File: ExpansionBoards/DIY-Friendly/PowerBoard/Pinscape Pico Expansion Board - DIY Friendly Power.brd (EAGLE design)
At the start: 138 x 102 mm, 87 parts, among them IC1 UCC27524P, IC10 ULN2803A, IC11 ULN2803A, IC12 ULN2803A, IC13 DS1307+, IC2 UCC27524P, IC3 UCC27524P, IC4 UCC27524P, IC5 UCC27524P, IC6 UCC27524P, IC7 UCC27524P, IC8 UCC27524P, IC9 ULN2803A, J1 640445-9, J2 640445-9, J3 640445-6, J4 1-640456-0, J5 1-640456-0, J6 1-640456-0, J7 1-640456-0, Q1 FDPF085N10A, Q10 FDPF085N10A, Q11 FDPF085N10A, Q12 FDPF085N10A, Q13 FDPF085N10A, Q14 FDPF085N10A, Q15 FDPF085N10A, Q16 FDPF085N10A, Q17 2N2222A, Q18 2N2222A, Q2 FDPF085N10A, Q3 FDPF085N10A, Q4 FDPF085N10A, Q5 FDPF085N10A, Q6 FDPF085N10A, Q7 FDPF085N10A, Q8 FDPF085N10A, Q9 FDPF085N10A, Y1 ECS-.327-12.5-13X-C

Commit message: BOM tweaks
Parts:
- Q1, Q10, Q11, Q12, Q13, Q14, Q15, Q16, Q2, Q3, Q4, Q5, Q6, Q7, Q8, Q9: value FDPF085N10A -> STP19NF20
- R1, R10, R11, R12, R14, R15, R16, R17, R2, R3, R4, R5, R6, R7, R8, R9: value 4R7 -> 200R

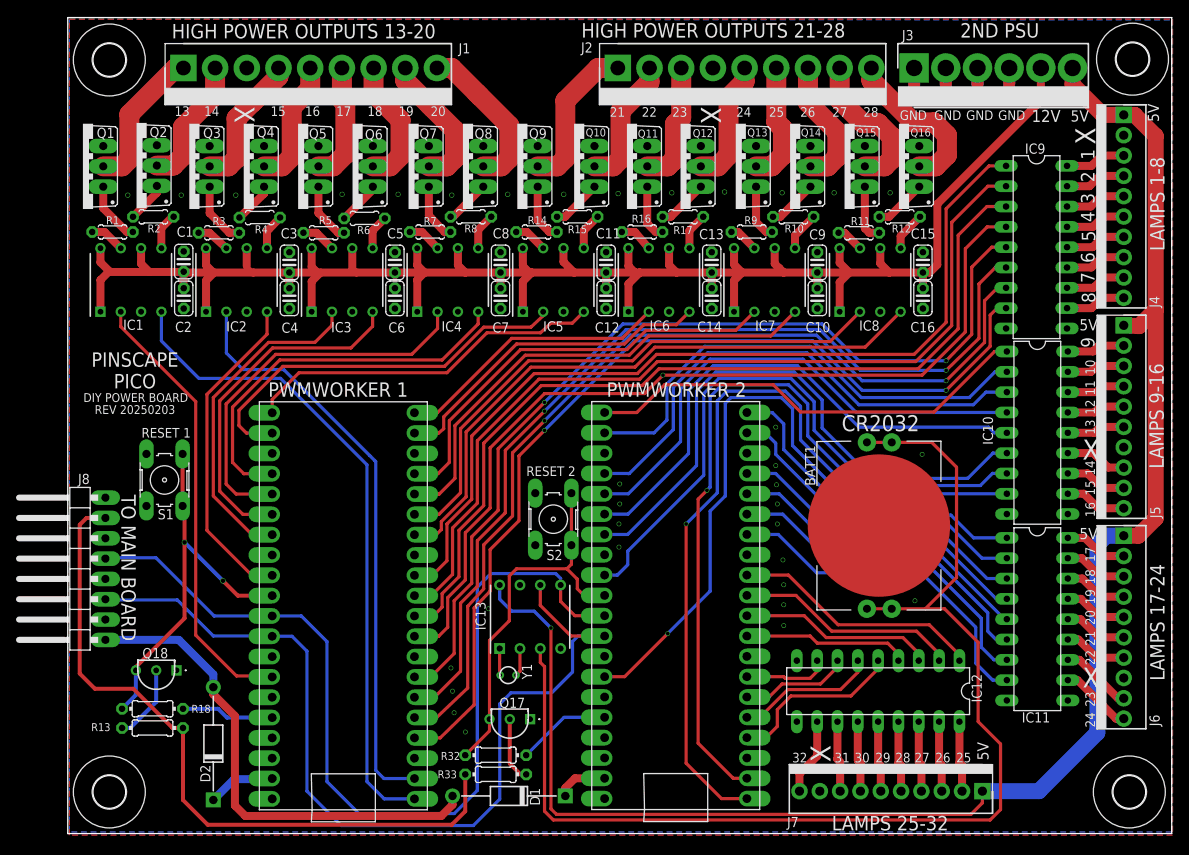
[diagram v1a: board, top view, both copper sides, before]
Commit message: exp board: DIY power: change battery holder to snap-in type
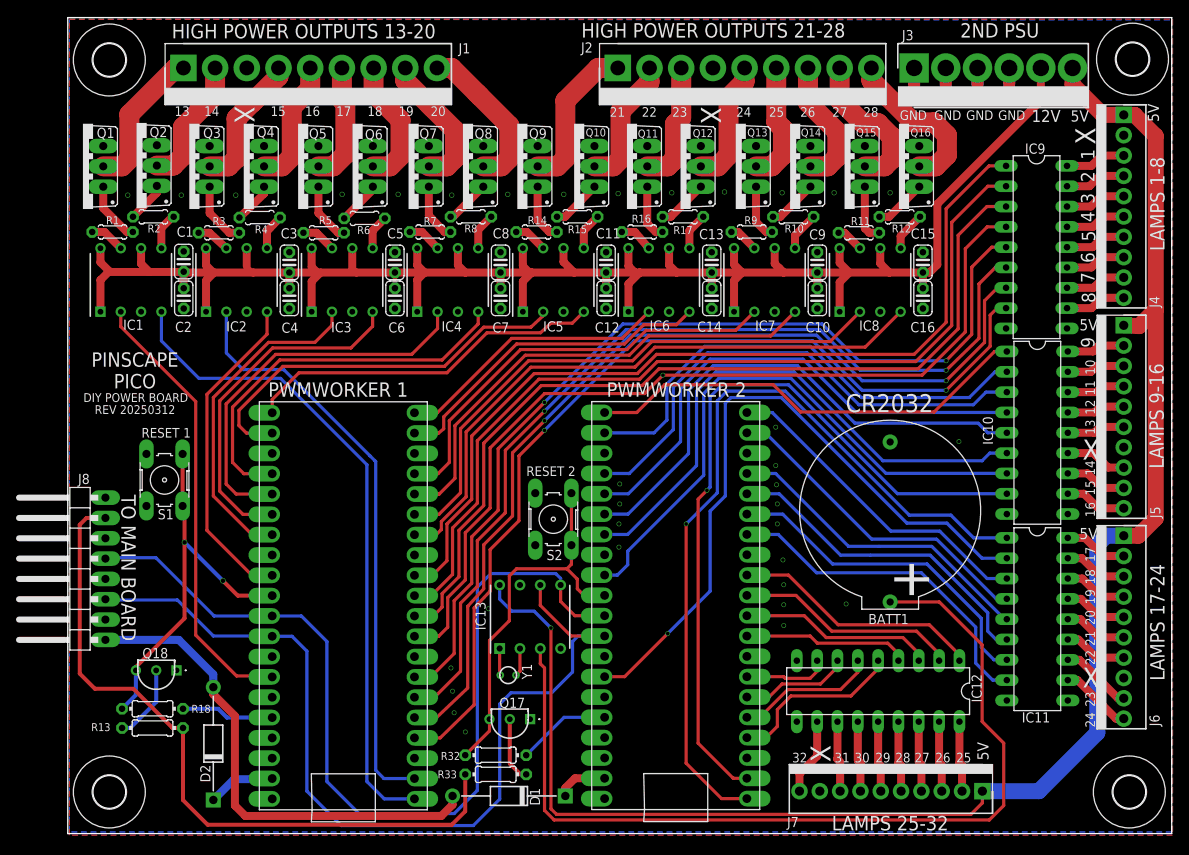
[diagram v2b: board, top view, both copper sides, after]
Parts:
- BATT1: value BAT-HLD-001-THM -> BH-123A-1; device SamacSys_Parts:BATHLD001THM -> SamacSys_Parts:BH-123A-1
- moved BATT1 2.36 mm to (102.8, 38.4), turned to 270 degrees
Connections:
- net GND: now also BATT1.-; no longer BATT1.5
- net N$35: now also BATT1.+; no longer BATT1.1, BATT1.2, BATT1.3, BATT1.4
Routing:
- net N$35: track 148.0 -> 114.0 mm
- net LAMPCTL14: track 73.0 -> 69.1 mm
- net LAMPCTL15: track 75.7 -> 72.4 mm
- net LAMPCTL18: track 88.4 -> 85.7 mm
- net LAMPCTL17: track 103.1 -> 100.6 mm
- net LAMPCTL16: track 97.5 -> 95.2 mm
- net LAMPCTL19: track 43.0 -> 41.1 mm
- net LAMPCTL20: track 41.9 -> 41.1 mm
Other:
- board text added: "REV 20250312"
- board text removed: "REV 20250203"

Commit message: exp board: power: change RTC power source to main Pico bus power
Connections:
- net 5V: no longer IC13.8
- net VBUS: now also IC13.8
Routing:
- net 5V: track 205.9 -> 117.4 mm, vias 1 -> 0
- net VBUS: track 62.2 -> 91.0 mm
- net N$40: track 48.7 -> 47.2 mm
- net GND: vias 34 -> 35
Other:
- board text added: "REV 20250325"
- board text removed: "REV 20250312"
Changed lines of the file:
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@@
 PICO</text>
 <text x="8.5" y="52.5" size="1.1" layer="25" ratio="20" rot="SR0" align="center">DIY POWER BOARD</text>
-<text x="8.4" y="51" size="1.1" layer="25" ratio="15" rot="SR0" align="center">REV 20250312</text>
+<text x="8.4" y="51" size="1.1" layer="25" ratio="15" rot="SR0" align="center">REV 20250325</text>
 <text x="29.5" y="98.3" size="1.8" layer="25" ratio="15" rot="SR0" align="center">HIGH POWER OUTPUTS 13-20</text>
 <text x="33.8" y="53.5" size="1.8" layer="25" ratio="15" rot="SR0" align="center">PWMWORKER 1</text>
@@
 <via x="89.5" y="29.1" extent="1-16" drill="0.45"/>
 <via x="89.4" y="32.2" extent="1-16" drill="0.45"/>
-<via x="49.7" y="10.7" extent="1-16" drill="0.45"/>
+<via x="49.5" y="11.1" extent="1-16" drill="0.45"/>
 <via x="48.3" y="13.1" extent="1-16" drill="0.45"/>
 <via x="48.1" y="15.8" extent="1-16" drill="0.45"/>
@@
 <via x="88.5" y="48.8" extent="1-16" drill="0.45"/>
 <contactref element="BATT1" pad="-"/>
+<via x="60.4" y="27" extent="1-16" drill="0.45"/>
 </signal>
 <signal name="SDA">
@@
 <wire x1="48.1" y1="2.7" x2="48.1" y2="1.6" width="1" layer="1"/>
 <wire x1="48.1" y1="1.6" x2="46.7" y2="0.2" width="1" layer="1"/>
+<contactref element="IC13" pad="8"/>
+<wire x1="48.1" y1="2.7" x2="48.1" y2="8" width="0.4" layer="1"/>
+<wire x1="48.1" y1="8" x2="51.6" y2="11.5" width="0.4" layer="1"/>
+<wire x1="51.6" y1="11.5" x2="51.6" y2="22.7" width="0.4" layer="1"/>
+<wire x1="51.6" y1="22.7" x2="53.99" y2="25.09" width="0.4" layer="1"/>
+<wire x1="53.99" y1="29.07" x2="53.99" y2="25.09" width="0.4" layer="1"/>
 </signal>
 <signal name="5V">
@@
 <wire x1="128.7" y1="34.1" x2="128.7" y2="10.6" width="2" layer="16"/>
 <wire x1="114.33" y1="3.3" x2="121.4" y2="3.3" width="2" layer="16"/>
-<contactref element="IC13" pad="8"/>
 <wire x1="125.6" y1="91.63" x2="129.4" y2="87.83" width="2" layer="1"/>
 <contactref element="J3" pad="6"/>
 <wire x1="125.6" y1="93.7" x2="125.6" y2="91.63" width="2" layer="1"/>
-<wire x1="114.33" y1="3.3" x2="114.33" y2="1.83" width="0.4" layer="1"/>
-<wire x1="61.1" y1="0.4" x2="112.9" y2="0.4" width="0.4" layer="1"/>
-<wire x1="60.4" y1="23.7" x2="58.3" y2="25.8" width="0.4" layer="16"/>
-<wire x1="53.99" y1="29.07" x2="53.99" y2="27.31" width="0.4" layer="16"/>
-<wire x1="53.99" y1="27.31" x2="55.5" y2="25.8" width="0.4" layer="16"/>
-<wire x1="55.5" y1="25.8" x2="58.3" y2="25.8" width="0.4" layer="16"/>
-<wire x1="60.4" y1="1.1" x2="61.1" y2="0.4" width="0.4" layer="1"/>
-<wire x1="60.4" y1="23.7" x2="60.4" y2="1.1" width="0.4" layer="1"/>
-<via x="60.4" y="23.7" extent="1-16" drill="0.45"/>
-<wire x1="112.9" y1="0.4" x2="114.33" y2="1.83" width="0.4" layer="1"/>
 <wire x1="128.7" y1="10.6" x2="121.4" y2="3.3" width="2" layer="16"/>
 </signal>
@@
 <contactref element="Q17" pad="3"/>
 <contactref element="PICO2" pad="RUN"/>
-<wire x1="55.2" y1="24.6" x2="55.2" y2="30.2" width="0.4" layer="1"/>
-<wire x1="55.2" y1="30.2" x2="56.1" y2="31.1" width="0.4" layer="1"/>
-<wire x1="56.1" y1="31.1" x2="62.4" y2="31.1" width="0.4" layer="1"/>
+<wire x1="58.7" y1="31.1" x2="62.4" y2="31.1" width="0.4" layer="1"/>
 <wire x1="62.4" y1="31.1" x2="63.7" y2="29.8" width="0.4" layer="1"/>
 <wire x1="63.7" y1="29.8" x2="63.7" y2="28.6" width="0.4" layer="1"/>
@@
 <wire x1="62.9606" y1="31.6606" x2="62.4" y2="31.1" width="0.4" layer="1"/>
 <wire x1="52.72" y1="12.3" x2="52.72" y2="22.12" width="0.4" layer="1"/>
-<wire x1="55.2" y1="24.6" x2="52.72" y2="22.12" width="0.4" layer="1"/>
 <wire x1="52.72" y1="12.3" x2="52.72" y2="10.83" width="0.4" layer="1"/>
 <wire x1="52.72" y1="10.83" x2="49.69" y2="7.8" width="0.4" layer="1"/>
+<wire x1="58.7" y1="31.1" x2="57.7" y2="30.1" width="0.4" layer="1"/>
+<wire x1="57.7" y1="30.1" x2="57.7" y2="27.1" width="0.4" layer="1"/>
+<wire x1="57.7" y1="27.1" x2="52.72" y2="22.12" width="0.4" layer="1"/>
 </signal>
 <signal name="N$41">

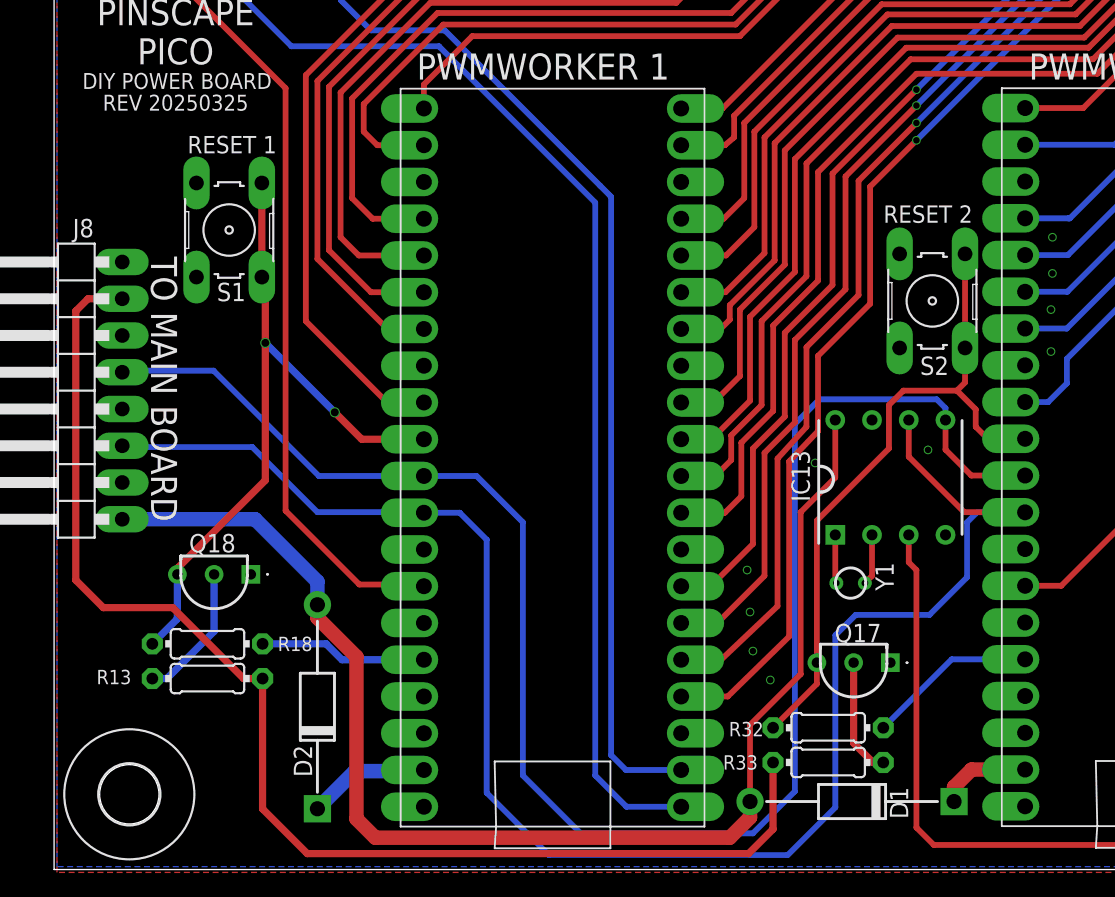
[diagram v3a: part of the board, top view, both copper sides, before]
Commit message: exp board: DIY power: add guard ring and isolated ground plane under DS1307 crystal per App Note 58
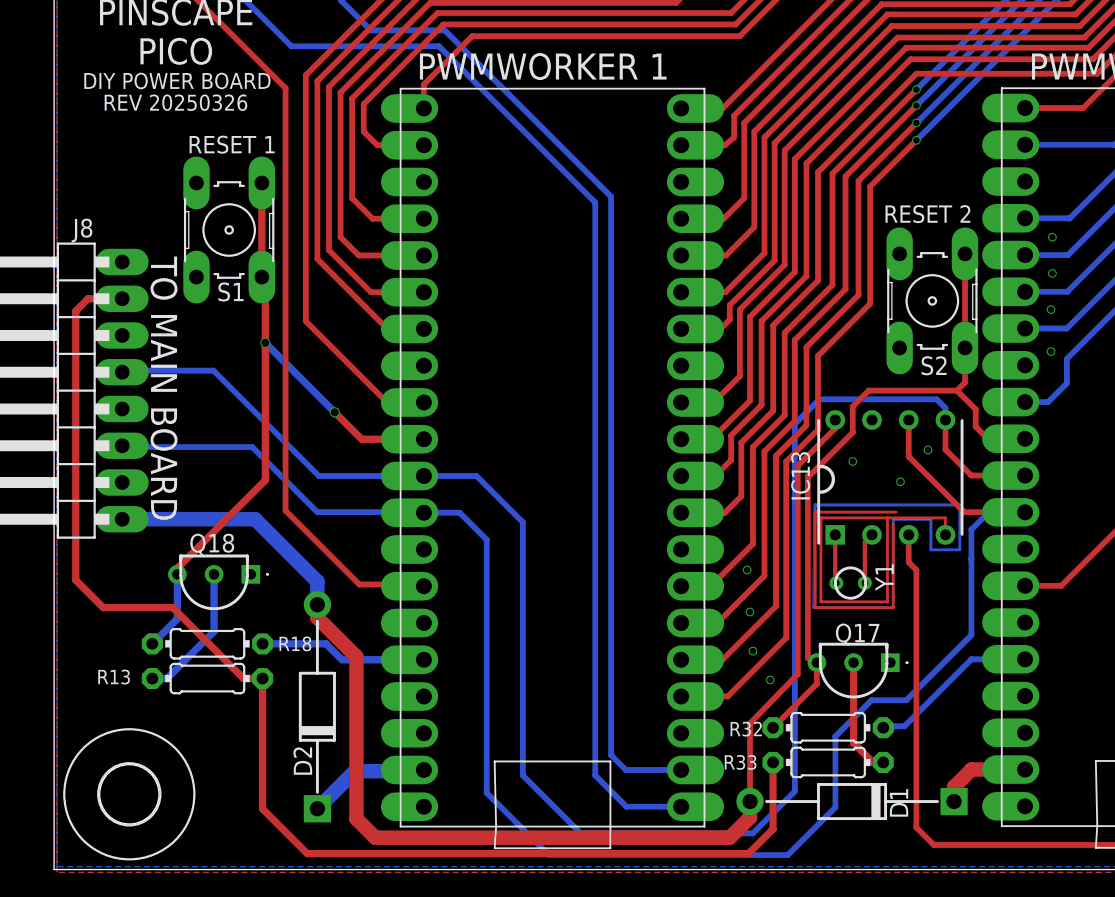
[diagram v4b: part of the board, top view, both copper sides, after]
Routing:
- net N$53: track 0.00 -> 37.9 mm
- net GND: track 17.1 -> 43.1 mm, vias 35 -> 36
- net N$52: track 0.00 -> 23.4 mm
- net N$40: track 47.2 -> 49.3 mm
- net SCL: track 115.6 -> 113.5 mm
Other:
- board text added: "REV 20250326"
- board text removed: "REV 20250325"
